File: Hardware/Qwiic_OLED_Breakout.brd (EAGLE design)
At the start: 27.3 x 29.2 mm, 28 parts

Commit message: Pre-design Review
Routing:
- net N$2: track 0.00 -> 4.85 mm, vias 0 -> 1
- net N$1: track 0.00 -> 4.83 mm, vias 0 -> 1
- net VDD: track 44.9 -> 48.4 mm

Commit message: Post Checklist Changes
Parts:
- removed U$1: (no value), SparkFun-Aesthetics:SFE_LOGO_NAME_.1
- added FID3, FID4: FIDUCIAL1X2, SparkFun-Aesthetics:FIDUCIAL-1X2
- moved LOGO4 71.8 mm to (4.57, 20.6)
- moved LOGO1 31.8 mm to (-6.35, -30.5)
- moved LOGO2 1.08 mm to (2.03, 0.76)
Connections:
- removed net VBAT: C6.1
- net VDD: now also C6.1
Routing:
- net VDD: track 48.4 -> 53.0 mm, vias 4 -> 5
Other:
- board text added: "Andy England"
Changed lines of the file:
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@@
 <setting verticaltext="up"/>
 </settings>
-<grid distance="30" unitdist="mil" unit="mil" style="lines" multiple="1" display="yes" altdistance="0.005" altunitdist="inch" altunit="inch"/>
+<grid distance="0.05" unitdist="inch" unit="inch" style="lines" multiple="1" display="yes" altdistance="0.005" altunitdist="inch" altunit="inch"/>
 <layers>
 <layer number="1" name="Top" color="4" fill="1" visible="yes" active="yes"/>
@@
 <layer number="15" name="Route15" color="4" fill="6" visible="no" active="no"/>
 <layer number="16" name="Bottom" color="1" fill="1" visible="yes" active="yes"/>
-<layer number="17" name="Pads" color="2" fill="1" visible="no" active="yes"/>
+<layer number="17" name="Pads" color="2" fill="1" visible="yes" active="yes"/>
 <layer number="18" name="Vias" color="2" fill="1" visible="yes" active="yes"/>
 <layer number="19" name="Unrouted" color="6" fill="1" visible="yes" active="yes"/>
 <layer number="20" name="Dimension" color="15" fill="1" visible="yes" active="yes"/>
-<layer number="21" name="tPlace" color="16" fill="1" visible="no" active="yes"/>
-<layer number="22" name="bPlace" color="14" fill="1" visible="no" active="yes"/>
-<layer number="23" name="tOrigins" color="15" fill="1" visible="no" active="yes"/>
+<layer number="21" name="tPlace" color="16" fill="1" visible="yes" active="yes"/>
+<layer number="22" name="bPlace" color="14" fill="1" visible="yes" active="yes"/>
+<layer number="23" name="tOrigins" color="15" fill="1" visible="yes" active="yes"/>
 <layer number="24" name="bOrigins" color="15" fill="1" visible="no" active="yes"/>
 <layer number="25" name="tNames" color="7" fill="1" visible="no" active="yes"/>
@@
 <layer number="37" name="tTest" color="7" fill="1" visible="no" active="yes"/>
 <layer number="38" name="bTest" color="7" fill="1" visible="no" active="yes"/>
-<layer number="39" name="tKeepout" color="4" fill="11" visible="no" active="yes"/>
-<layer number="40" name="bKeepout" color="1" fill="11" visible="no" active="yes"/>
+<layer number="39" name="tKeepout" color="4" fill="11" visible="yes" active="yes"/>
+<layer number="40" name="bKeepout" color="1" fill="11" visible="yes" active="yes"/>
 <layer number="41" name="tRestrict" color="4" fill="10" visible="no" active="yes"/>
 <layer number="42" name="bRestrict" color="1" fill="10" visible="no" active="yes"/>
@@
 <layer number="45" name="Holes" color="7" fill="1" visible="no" active="yes"/>
 <layer number="46" name="Milling" color="3" fill="1" visible="no" active="yes"/>
-<layer number="47" name="Measures" color="7" fill="1" visible="no" active="yes"/>
+<layer number="47" name="Measures" color="7" fill="1" visible="yes" active="yes"/>
 <layer number="48" name="Document" color="7" fill="1" visible="no" active="yes"/>
 <layer number="49" name="Reference" color="7" fill="1" visible="no" active="yes"/>
 <layer number="50" name="dxf" color="7" fill="1" visible="no" active="no"/>
-<layer number="51" name="tDocu" color="6" fill="1" visible="no" active="yes"/>
+<layer number="51" name="tDocu" color="6" fill="1" visible="yes" active="yes"/>
 <layer number="52" name="bDocu" color="7" fill="1" visible="no" active="yes"/>
 <layer number="53" name="tGND_GNDA" color="7" fill="1" visible="no" active="no"/>
@@
 <wire x1="14.163040625" y1="25.054559375" x2="14.163040625" y2="29.21" width="0.2032" layer="20"/>
 <wire x1="14.163040625" y1="29.21" x2="23.749" y2="29.21" width="0.2032" layer="20"/>
-<text x="13.97" y="-27.94" size="1.778" layer="51" font="vector" ratio="10">Joel Bartlett</text>
+<text x="8.89" y="-27.94" size="1.778" layer="51" font="vector">Joel Bartlett</text>
 <hole x="2.286" y="20.574" drill="0.381"/>
 <hole x="3.048" y="20.574" drill="0.381"/>
@@
 <hole x="17.526" y="20.574" drill="0.381"/>
 <hole x="18.288" y="20.574" drill="0.381"/>
+<dimension x1="-3.81" y1="29.21" x2="-3.81" y2="0" x3="-13.97" y3="14.605" textsize="1.778" layer="47" unit="inch"/>
+<dimension x1="-3.556" y1="29.21" x2="23.749" y2="29.21" x3="10.0965" y3="36.83" textsize="1.778" layer="47" unit="inch"/>
+<dimension x1="-0.635" y1="26.67" x2="20.955" y2="26.67" x3="10.16" y3="31.75" textsize="1.778" layer="47" unit="inch"/>
+<dimension x1="0" y1="0" x2="0" y2="26.67" x3="-7.62" y3="13.335" textsize="1.778" layer="47" unit="inch"/>
+<text x="12.7" y="-30.48" size="1.778" layer="51" font="vector">Andy England</text>
 </plain>
 <attributes>
@@
 <element name="H2" library="SparkFun-Hardware" package="STAND-OFF" value="STAND-OFF" x="-0.635" y="26.67"/>
 <element name="JP3" library="SparkFun-Jumpers" package="SMT-JUMPER_2_NO_SILK" value="" x="12.7" y="12.7"/>
-<element name="LOGO1" library="SparkFun-Aesthetics" package="REVISION" value="REVISION" x="-38.1" y="-31.75"/>
-<element name="LOGO2" library="SparkFun-Aesthetics" package="SFE_LOGO_FLAME_.1" value="SFE_LOGO_FLAME.1_INCH" x="1.27" y="0"/>
-<element name="U$1" library="SparkFun-Aesthetics" package="SFE_LOGO_NAME_.1" value="" x="4.191" y="20.32"/>
-<element name="LOGO4" library="SparkFun-Aesthetics" package="SFE_LOGO_NAME_.1" value="SFE_LOGO_NAME.1_INCH" x="-38.862" y="-36.576"/>
+<element name="LOGO1" library="SparkFun-Aesthetics" package="REVISION" value="REVISION" x="-6.35" y="-30.48"/>
+<element name="LOGO2" library="SparkFun-Aesthetics" package="SFE_LOGO_FLAME_.1" value="SFE_LOGO_FLAME.1_INCH" x="2.032" y="0.762"/>
+<element name="LOGO4" library="SparkFun-Aesthetics" package="SFE_LOGO_NAME_.1" value="SFE_LOGO_NAME.1_INCH" x="4.572" y="20.574"/>
+<element name="FID3" library="SparkFun-Aesthetics" package="FIDUCIAL-1X2" value="FIDUCIAL1X2" x="1.27" y="15.875" rot="MR0"/>
+<element name="FID4" library="SparkFun-Aesthetics" package="FIDUCIAL-1X2" value="FIDUCIAL1X2" x="19.05" y="1.27" rot="MR0"/>
 </elements>
 <signals>
@@
 <wire x1="14.478" y1="5.715" x2="14.478" y2="7.09" width="0.2032" layer="16"/>
 <wire x1="14.478" y1="7.09" x2="14.5" y2="7.112" width="0.2032" layer="16"/>
+<contactref element="C6" pad="1"/>
+<wire x1="15.24" y1="7.405" x2="15.24" y2="5.08" width="0.2032" layer="1"/>
+<via x="15.24" y="5.08" extent="1-16" drill="0.381"/>
+<wire x1="15.24" y1="5.08" x2="15.8" y2="5.64" width="0.2032" layer="16"/>
+<wire x1="15.8" y1="5.64" x2="15.8" y2="7.112" width="0.2032" layer="16"/>
 </signal>
 <signal name="VCOMH">
@@
 <wire x1="17.1" y1="5.506" x2="17.1" y2="7.112" width="0.254" layer="16"/>
 </signal>
-<signal name="VBAT">
-<contactref element="C6" pad="1"/>
-</signal>
 <signal name="VCC">
 <contactref element="OLED1" pad="26"/>
@@
 <contactref element="R3" pad="1"/>
 <wire x1="11.25" y1="7.112" x2="11.25" y2="5.641" width="0.254" layer="16"/>
-<via x="13.335" y="4.572" extent="1-16" drill="0.508"/>
+<via x="13.335" y="4.572" extent="1-16" drill="0.381"/>
 <wire x1="13.335" y1="7.405" x2="13.374" y2="7.366" width="0.254" layer="1"/>
 <wire x1="13.374" y1="7.366" x2="13.97" y2="7.366" width="0.254" layer="1"/>

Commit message: Checklist
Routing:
- net VDD: track 53.0 -> 50.5 mm
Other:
- board text added: "v10"
- board text removed: "v01"

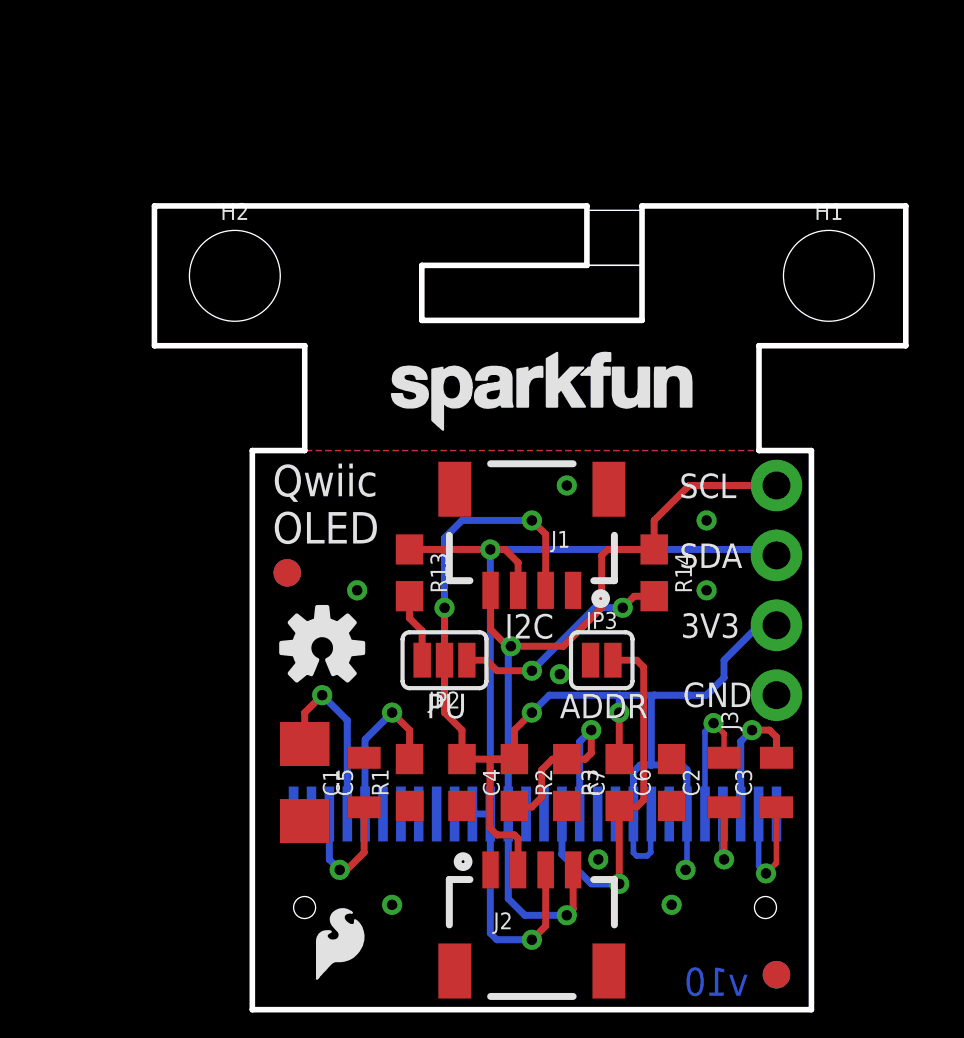
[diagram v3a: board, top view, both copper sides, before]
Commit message: Checklist issues fixed
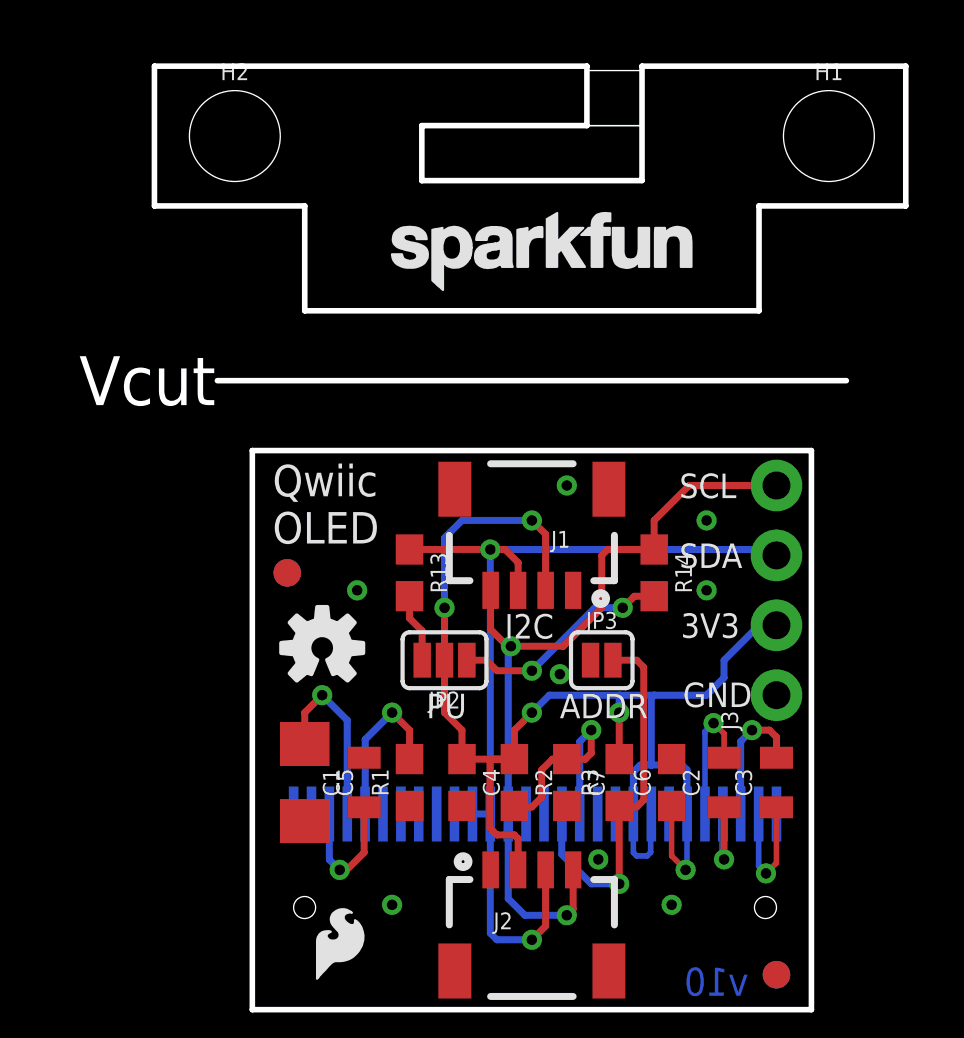
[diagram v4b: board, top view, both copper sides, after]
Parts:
- moved H1 5.08 mm to (21.0, 31.8)
- moved H2 5.08 mm to (-0.64, 31.8)
- moved LOGO4 5.08 mm to (4.57, 25.7)
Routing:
- net VDD: track 50.5 -> 52.9 mm
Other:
- board size 27.3 x 29.2 mm -> 27.3 x 34.3 mm
- board text added: "Vcut"
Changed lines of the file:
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@@
 <text x="17.78" y="18.5928" size="0.889" layer="22" font="vector" ratio="15" rot="MR0">SCL</text>
 <wire x1="20.32" y1="0" x2="20.32" y2="20.32" width="0.2032" layer="20"/>
-<wire x1="20.32" y1="20.32" x2="18.415" y2="20.32" width="0.2032" layer="20"/>
-<wire x1="1.905" y1="20.32" x2="0" y2="20.32" width="0.2032" layer="20"/>
 <wire x1="0" y1="20.32" x2="0" y2="0" width="0.2032" layer="20"/>
 <wire x1="0" y1="0" x2="20.32" y2="0" width="0.2032" layer="20"/>
-<wire x1="-3.556" y1="29.21" x2="-3.556" y2="24.13" width="0.2032" layer="20"/>
-<wire x1="-3.556" y1="24.13" x2="1.905" y2="24.13" width="0.2032" layer="20"/>
-<wire x1="18.415" y1="24.13" x2="23.749" y2="24.13" width="0.2032" layer="20"/>
-<wire x1="23.749" y1="24.13" x2="23.749" y2="29.21" width="0.2032" layer="20"/>
-<wire x1="1.905" y1="20.32" x2="1.905" y2="24.13" width="0.2032" layer="20"/>
-<wire x1="18.415" y1="24.13" x2="18.415" y2="20.32" width="0.2032" layer="20"/>
-<rectangle x1="6.16" y1="25.05" x2="14.16" y2="27.05" layer="46" rot="R180"/>
-<rectangle x1="12.16" y1="27.05" x2="14.16" y2="29.05" layer="46" rot="R180"/>
-<wire x1="12.16" y1="29.21" x2="12.16" y2="27.05" width="0.2032" layer="20"/>
-<wire x1="12.16" y1="27.05" x2="6.16" y2="27.05" width="0.2032" layer="20"/>
-<wire x1="6.16" y1="27.05" x2="6.16" y2="25.05" width="0.2032" layer="20"/>
-<wire x1="6.16" y1="25.05" x2="14.16" y2="25.05" width="0.2032" layer="20"/>
-<wire x1="12.16" y1="29.21" x2="-3.556" y2="29.21" width="0.2032" layer="20"/>
-<wire x1="14.163040625" y1="25.054559375" x2="14.163040625" y2="29.21" width="0.2032" layer="20"/>
-<wire x1="14.163040625" y1="29.21" x2="23.749" y2="29.21" width="0.2032" layer="20"/>
+<wire x1="-3.556" y1="34.29" x2="-3.556" y2="29.21" width="0.2032" layer="20"/>
+<wire x1="-3.556" y1="29.21" x2="1.905" y2="29.21" width="0.2032" layer="20"/>
+<wire x1="18.415" y1="29.21" x2="23.749" y2="29.21" width="0.2032" layer="20"/>
+<wire x1="23.749" y1="29.21" x2="23.749" y2="34.29" width="0.2032" layer="20"/>
+<rectangle x1="6.16" y1="30.13" x2="14.16" y2="32.13" layer="46" rot="R180"/>
+<rectangle x1="12.16" y1="32.13" x2="14.16" y2="34.13" layer="46" rot="R180"/>
+<wire x1="12.16" y1="34.29" x2="12.16" y2="32.13" width="0.2032" layer="20"/>
+<wire x1="12.16" y1="32.13" x2="6.16" y2="32.13" width="0.2032" layer="20"/>
+<wire x1="6.16" y1="32.13" x2="6.16" y2="30.13" width="0.2032" layer="20"/>
+<wire x1="6.16" y1="30.13" x2="14.16" y2="30.13" width="0.2032" layer="20"/>
+<wire x1="12.16" y1="34.29" x2="-3.556" y2="34.29" width="0.2032" layer="20"/>
+<wire x1="14.163040625" y1="30.134559375" x2="14.163040625" y2="34.29" width="0.2032" layer="20"/>
+<wire x1="14.163040625" y1="34.29" x2="23.749" y2="34.29" width="0.2032" layer="20"/>
 <text x="8.89" y="-27.94" size="1.778" layer="51" font="vector">Joel Bartlett</text>
-<dimension x1="-3.81" y1="29.21" x2="-3.81" y2="0" x3="-13.97" y3="14.605" textsize="1.778" layer="47" unit="inch"/>
-<dimension x1="-3.556" y1="29.21" x2="23.749" y2="29.21" x3="10.0965" y3="36.83" textsize="1.778" layer="47" unit="inch"/>
-<dimension x1="-0.635" y1="26.67" x2="20.955" y2="26.67" x3="10.16" y3="31.75" textsize="1.778" layer="47" unit="inch"/>
-<dimension x1="0" y1="0" x2="0" y2="26.67" x3="-7.62" y3="13.335" textsize="1.778" layer="47" unit="inch"/>
+<dimension x1="-3.81" y1="34.29" x2="-3.81" y2="0" x3="-15.24" y3="17.145" textsize="1.778" layer="47" unit="inch"/>
+<dimension x1="-3.556" y1="34.29" x2="23.749" y2="34.29" x3="10.0965" y3="40.64" textsize="1.778" layer="47" unit="inch"/>
+<dimension x1="-0.635" y1="31.75" x2="20.955" y2="31.75" x3="10.16" y3="36.83" textsize="1.778" layer="47" unit="inch"/>
+<dimension x1="0" y1="0" x2="0" y2="31.75" x3="-11.43" y3="15.875" textsize="1.778" layer="47" unit="inch"/>
 <text x="12.7" y="-30.48" size="1.778" layer="51" font="vector">Andy England</text>
-<wire x1="-1.27" y1="20.32" x2="21.59" y2="20.32" width="0.2032" layer="102"/>
+<wire x1="-1.27" y1="22.86" x2="21.59" y2="22.86" width="0.2032" layer="20"/>
+<wire x1="1.905" y1="29.21" x2="1.905" y2="25.4" width="0.2032" layer="20"/>
+<wire x1="1.905" y1="25.4" x2="18.415" y2="25.4" width="0.2032" layer="20"/>
+<wire x1="18.415" y1="25.4" x2="18.415" y2="29.21" width="0.2032" layer="20"/>
+<wire x1="0" y1="20.32" x2="20.32" y2="20.32" width="0.2032" layer="20"/>
+<text x="-3.81" y="22.86" size="1.778" layer="20" align="center">Vcut</text>
+<dimension x1="-6.35" y1="22.86" x2="-6.35" y2="0" x3="-7.62" y3="11.43" textsize="1.778" layer="20" unit="inch"/>
 </plain>
 <attributes>
@@
 </element>
 <element name="JP2" library="SparkFun-Jumpers" package="SMT-JUMPER_3_2-NC_PASTE_SILK" value="" x="6.985" y="12.7" rot="R180"/>
-<element name="H1" library="SparkFun-Hardware" package="STAND-OFF" value="STAND-OFF" x="20.955" y="26.67"/>
-<element name="H2" library="SparkFun-Hardware" package="STAND-OFF" value="STAND-OFF" x="-0.635" y="26.67"/>
+<element name="H1" library="SparkFun-Hardware" package="STAND-OFF" value="STAND-OFF" x="20.955" y="31.75"/>
+<element name="H2" library="SparkFun-Hardware" package="STAND-OFF" value="STAND-OFF" x="-0.635" y="31.75"/>
 <element name="JP3" library="SparkFun-Jumpers" package="SMT-JUMPER_2_NO_SILK" value="" x="12.7" y="12.7"/>
 <element name="LOGO1" library="SparkFun-Aesthetics" package="REVISION" value="REVISION" x="-6.35" y="-30.48"/>
 <element name="LOGO2" library="SparkFun-Aesthetics" package="SFE_LOGO_FLAME_.1" value="SFE_LOGO_FLAME.1_INCH" x="2.032" y="0.762"/>
-<element name="LOGO4" library="SparkFun-Aesthetics" package="SFE_LOGO_NAME_.1" value="SFE_LOGO_NAME.1_INCH" x="4.572" y="20.574"/>
+<element name="LOGO4" library="SparkFun-Aesthetics" package="SFE_LOGO_NAME_.1" value="SFE_LOGO_NAME.1_INCH" x="4.572" y="25.654"/>
 <element name="FID3" library="SparkFun-Aesthetics" package="FIDUCIAL-1X2" value="FIDUCIAL1X2" x="1.27" y="15.875" rot="MR0"/>
 <element name="FID4" library="SparkFun-Aesthetics" package="FIDUCIAL-1X2" value="FIDUCIAL1X2" x="19.05" y="1.27" rot="MR0"/>
@@
 <via x="10.16" y="10.795" extent="1-16" drill="0.381"/>
 <wire x1="13.335" y1="11.43" x2="13.335" y2="10.795" width="0.254" layer="16"/>
-<wire x1="15.875" y1="11.43" x2="14.605" y2="11.43" width="0.254" layer="16"/>
+<wire x1="16.51" y1="11.43" x2="14.605" y2="11.43" width="0.254" layer="16"/>
 <wire x1="14.605" y1="11.43" x2="13.335" y2="11.43" width="0.254" layer="16"/>
 <wire x1="14.5" y1="11.325" x2="14.605" y2="11.43" width="0.254" layer="16"/>
-<wire x1="15.8" y1="11.355" x2="15.875" y2="11.43" width="0.254" layer="16"/>
 <wire x1="18.415" y1="13.97" x2="19.05" y2="13.97" width="0.254" layer="16"/>
 <wire x1="13.335" y1="11.43" x2="10.795" y2="11.43" width="0.254" layer="16"/>
 <wire x1="10.795" y1="11.43" x2="10.16" y2="10.795" width="0.254" layer="16"/>
-<wire x1="15.875" y1="11.43" x2="16.51" y2="11.43" width="0.254" layer="16"/>
 <wire x1="16.51" y1="11.43" x2="17.145" y2="12.065" width="0.254" layer="16"/>
 <wire x1="17.145" y1="12.065" x2="17.145" y2="12.7" width="0.254" layer="16"/>
@@
 <wire x1="15.748" y1="5.08" x2="15.8" y2="5.132" width="0.2032" layer="16"/>
 <wire x1="15.8" y1="5.132" x2="15.8" y2="7.112" width="0.2032" layer="16"/>
-<wire x1="15.8" y1="7.112" x2="15.24" y2="7.405" width="0" layer="19" extent="1-16"/>
+<wire x1="15.24" y1="7.405" x2="15.24" y2="5.588" width="0.2032" layer="1"/>
+<wire x1="15.24" y1="5.588" x2="15.748" y2="5.08" width="0.2032" layer="1"/>
 </signal>
 <signal name="VCOMH">
